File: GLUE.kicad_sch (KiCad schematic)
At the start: 13 parts

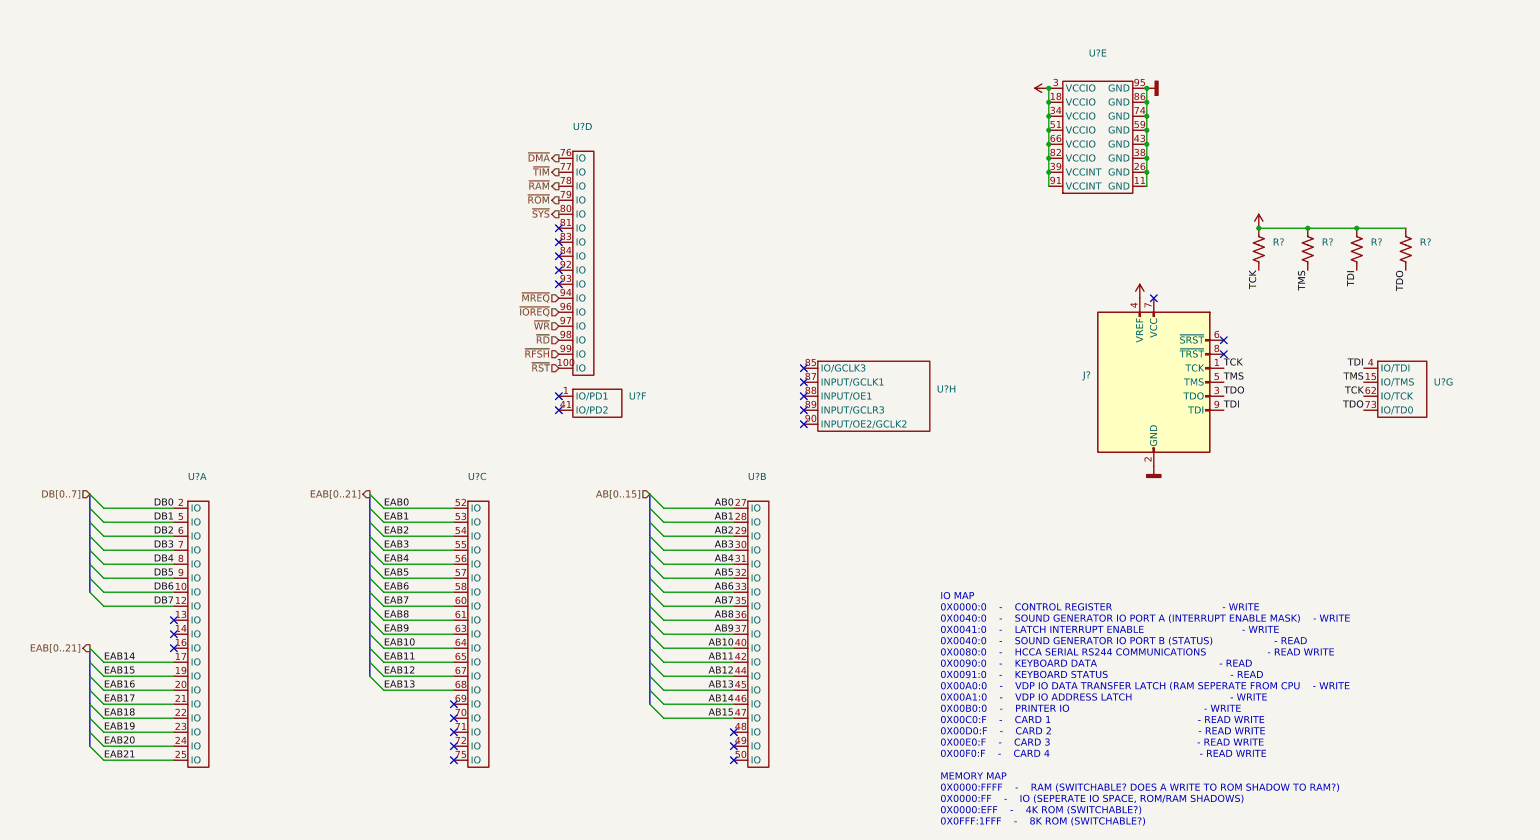
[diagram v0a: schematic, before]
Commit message: updated 84c10 pinout, apparently never checked for validity.... further simplification of dma and timer system (removed mode 2 interrupt structure, and interrupts in general) cleaned up vhdl code for 1508, still need testing to ensure functionality and that it even fits in the 1508....
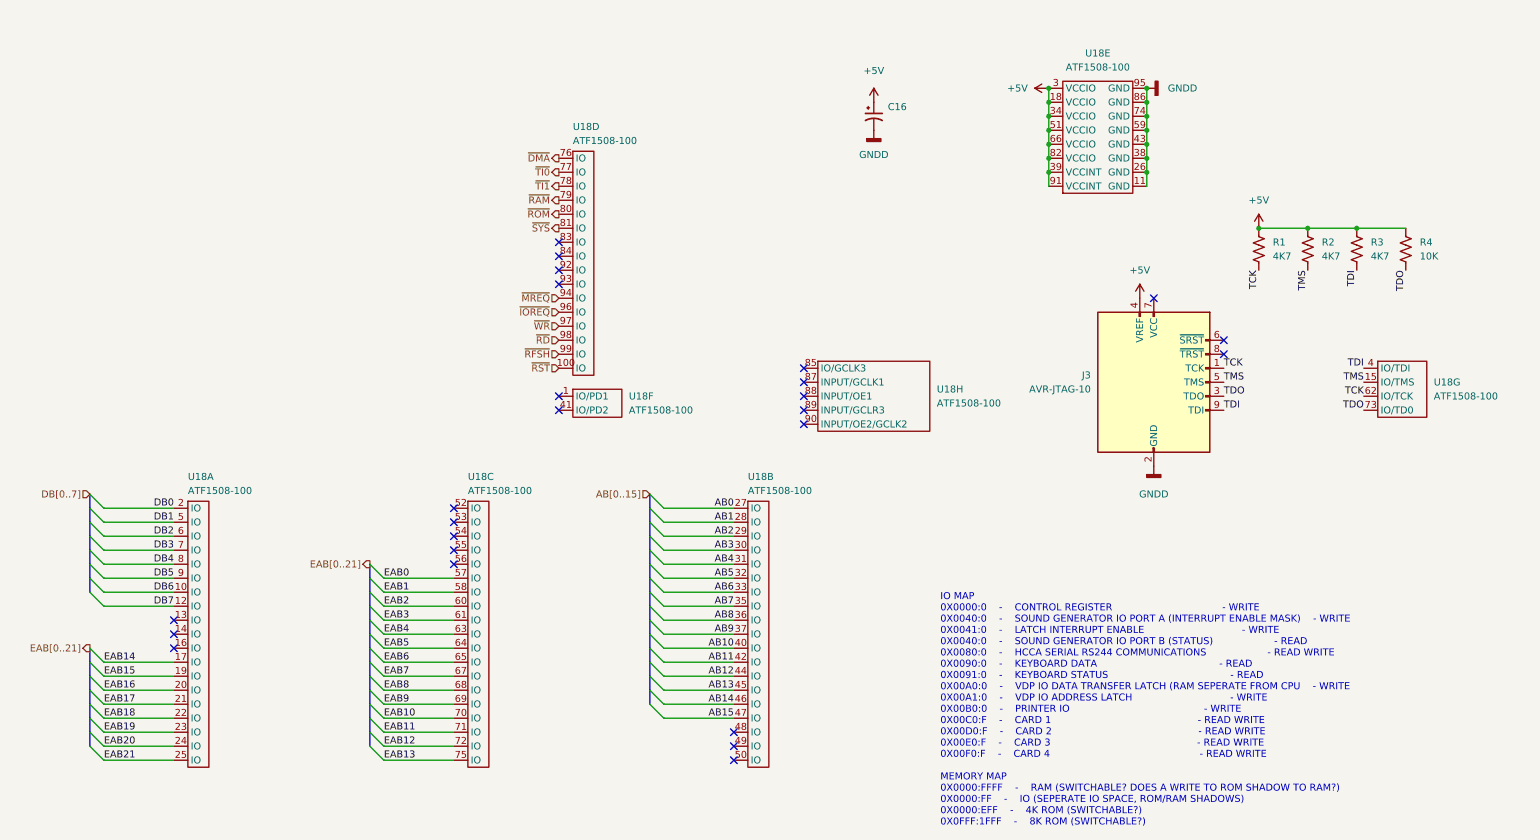
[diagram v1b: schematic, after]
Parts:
- added C16: (no value), symbol Device:C_Polarized_Small_US
- J3: renamed from J?; value (none) -> AVR-JTAG-10; footprint (none) -> Connector_IDC:IDC-Header_2x05_P2.54mm_Horizontal
- R1, R2, R3: renamed from R?; value (none) -> 4K7; footprint (none) -> Resistor_SMD:R_0603_1608Metric
- R4: renamed from R?; value (none) -> 10K; footprint (none) -> Resistor_SMD:R_0603_1608Metric
- U18: renamed from U?; value (none) -> ATF1508-100; footprint (none) -> Package_QFP:TQFP-144_16x16mm_P0.4mm
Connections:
- net +5V: now also C16.1
- net EAB0: now also U18.57 (IO); no longer U18.52 (IO)
- net EAB1: now also U18.58 (IO); no longer U18.53 (IO)
- net EAB10: now also U18.70 (IO); no longer U18.64 (IO)
- net EAB11: now also U18.71 (IO); no longer U18.65 (IO)
- net EAB12: now also U18.72 (IO); no longer U18.67 (IO)
- net EAB13: now also U18.75 (IO); no longer U18.68 (IO)
- net EAB2: now also U18.60 (IO); no longer U18.54 (IO)
- net EAB3: now also U18.61 (IO); no longer U18.55 (IO)
- net EAB4: now also U18.63 (IO); no longer U18.56 (IO)
- net EAB5: now also U18.64 (IO); no longer U18.57 (IO)
- net EAB6: now also U18.65 (IO); no longer U18.58 (IO)
- net EAB7: now also U18.67 (IO); no longer U18.60 (IO)
- net EAB8: now also U18.68 (IO); no longer U18.61 (IO)
- net EAB9: now also U18.69 (IO); no longer U18.63 (IO)
- net GNDD: now also C16.2
- net ~{RAM}: now also U18.79 (IO); no longer U18.78 (IO)
- net ~{ROM}: now also U18.80 (IO); no longer U18.79 (IO)
- net ~{SYS}: now also U18.81 (IO); no longer U18.80 (IO)
- net ~{TIM} renamed ~{TI0}
- new net ~{TI1}: U18.78 (IO)
- no-connect marks 26 -> 25

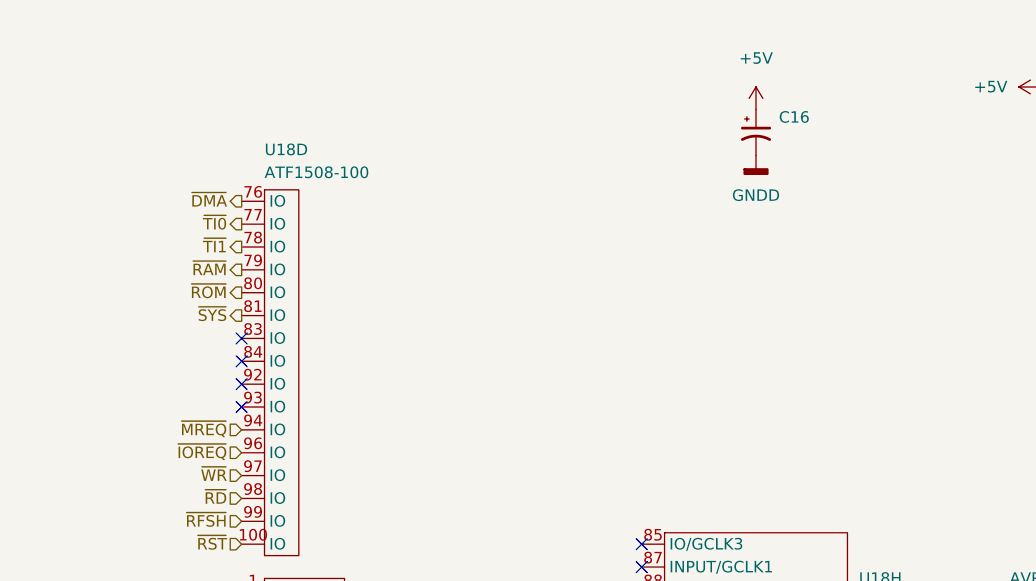
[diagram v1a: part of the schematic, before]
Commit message: forgot to actually add the previous fixes to kicad
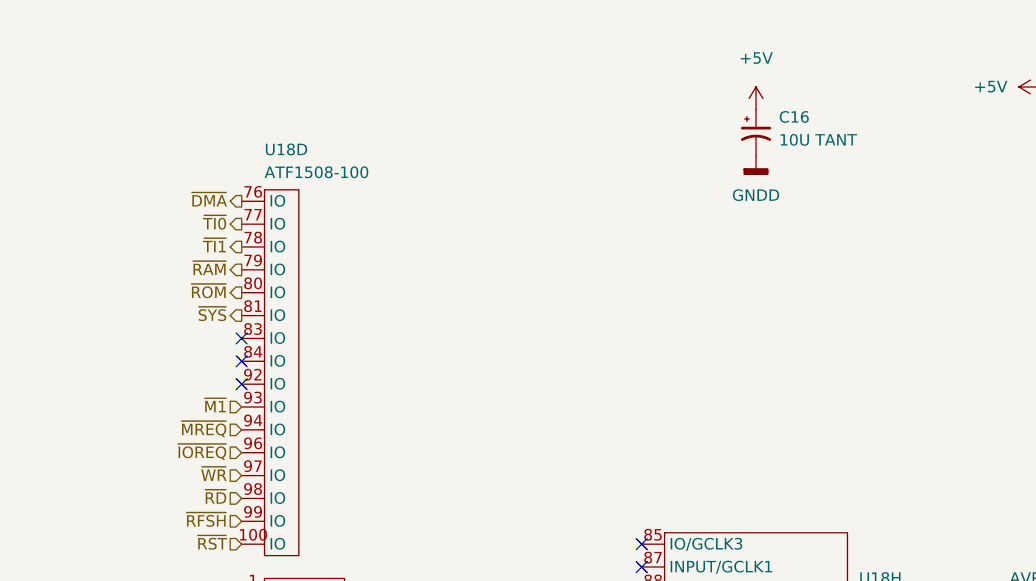
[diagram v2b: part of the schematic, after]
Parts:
- C16: value (none) -> 10U TANT; footprint (none) -> Capacitor_Tantalum_SMD:CP_EIA-3528-15_AVX-H
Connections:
- net ~{M1}: now reaches U18.93 (IO)
- no-connect marks 25 -> 24
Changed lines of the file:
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@@
   (no_connect (at 38.1 128.27))
   (no_connect (at 139.7 153.67))
-  (no_connect (at 107.95 67.31))
   (no_connect (at 88.9 113.03))
   (no_connect (at 107.95 87.63))
@@
     (effects (font (size 1.27 1.27)) (justify right))
   )
+  (hierarchical_label "~{M1}" (shape input) (at 107.95 67.31 180)
+    (effects (font (size 1.27 1.27)) (justify right))
+  )
   (hierarchical_label "~{TI0}" (shape output) (at 107.95 46.99 180)
     (effects (font (size 1.27 1.27)) (justify right))
@@
       (effects (font (size 1.27 1.27)) (justify left))
     )
-    (property "Value" "" (id 1) (at 167.64 37.6681 0)
-      (effects (font (size 1.27 1.27)) (justify left))
-    )
-    (property "Footprint" "" (id 2) (at 165.1 36.83 0)
+    (property "Value" "10U TANT" (id 1) (at 167.64 37.6681 0)
+      (effects (font (size 1.27 1.27)) (justify left))
+    )
+    (property "Footprint" "Capacitor_Tantalum_SMD:CP_EIA-3528-15_AVX-H" (id 2) (at 165.1 36.83 0)
       (effects (font (size 1.27 1.27)) hide)
     )
@@
     (pin "90")
   )
+  (sheet_instances
+    (path "/" (page "1"))
+  )
+  (symbol_instances
+    (path "/7434df1e-8c76-43d0-ba69-cff4ade1af5e"
+      (reference "#PWR094") (unit 1) (value "+5V") (footprint "")
+    )
+    (path "/7de21762-bfdd-4bb2-b954-a7695409df25"
+      (reference "#PWR095") (unit 1) (value "GNDD") (footprint "")
+    )
+    (path "/9c164401-27a9-4d88-be66-43af1a76f3eb"
+      (reference "#PWR096") (unit 1) (value "+5V") (footprint "")
+    )
+    (path "/93ac4910-c1f5-4a01-87b0-acf747d47f0e"
+      (reference "#PWR097") (unit 1) (value "+5V") (footprint "")
+    )
+    (path "/df39298e-6841-46be-bdf6-2826667bc816"
+      (reference "#PWR098") (unit 1) (value "GNDD") (footprint "")
+    )
+    (path "/75ef9d2a-dff4-43fc-9bd8-d0daa9f5c7c0"
+      (reference "#PWR099") (unit 1) (value "GNDD") (footprint "")
+    )
+    (path "/3f1d090d-9c55-4c35-80c5-c0ffce26f264"
+      (reference "#PWR0100") (unit 1) (value "+5V") (footprint "")
+    )
+    (path "/2a6e4ede-8be7-4625-a308-e5070c6ce3b0"
+      (reference "C16") (unit 1) (value "~") (footprint "")
+    )
+    (path "/7dae750f-5ca2-42a0-a992-9bacb9e63901"
+      (reference "J3") (unit 1) (value "AVR-JTAG-10") (footprint "Connector_IDC:IDC-Header_2x05_P2.54mm_Horizontal")
+    )
+    (path "/737b265f-12ab-4831-9a3d-17a7941c355c"
+      (reference "R1") (unit 1) (value "4K7") (footprint "Resistor_SMD:R_0603_1608Metric")
+    )
+    (path "/d143b373-f908-4728-b1a9-27bef0529792"
+      (reference "R2") (unit 1) (value "4K7") (footprint "Resistor_SMD:R_0603_1608Metric")
+    )
+    (path "/5535c419-0d51-45cd-9540-fecebe275496"
+      (reference "R3") (unit 1) (value "4K7") (footprint "Resistor_SMD:R_0603_1608Metric")
+    )
+    (path "/d91b456a-f3e0-43ba-9cb7-46edc063d27a"
+      (reference "R4") (unit 1) (value "10K") (footprint "Resistor_SMD:R_0603_1608Metric")
+    )
+    (path "/eac06b71-dbc2-4ad8-929e-1eb79d804427"
+      (reference "U18") (unit 1) (value "ATF1508-100") (footprint "Package_QFP:TQFP-144_16x16mm_P0.4mm")
+    )
+    (path "/600f8de0-3f16-43a2-b197-38b4e9654d87"
+      (reference "U18") (unit 2) (value "ATF1508-100") (footprint "Package_QFP:TQFP-144_16x16mm_P0.4mm")
+    )
+    (path "/d931fdbc-0cfb-4122-9f70-a852ebf6cf8e"
+      (reference "U18") (unit 3) (value "ATF1508-100") (footprint "Package_QFP:TQFP-144_16x16mm_P0.4mm")
+    )
+    (path "/ec3cefd2-bab6-4b6d-88f5-ba74a67c8eb2"
+      (reference "U18") (unit 4) (value "ATF1508-100") (footprint "Package_QFP:TQFP-144_16x16mm_P0.4mm")
+    )
+    (path "/5b869971-68f3-406b-a43a-58d32abb29a3"
+      (reference "U18") (unit 5) (value "ATF1508-100") (footprint "Package_QFP:TQFP-144_16x16mm_P0.4mm")
+    )
+    (path "/ae7cd84e-81ac-48d4-89cd-9fc94aeaef33"
+      (reference "U18") (unit 6) (value "ATF1508-100") (footprint "Package_QFP:TQFP-144_16x16mm_P0.4mm")
+    )
+    (path "/7199891f-146f-4ca3-92f9-5dadccfd3e4a"
+      (reference "U18") (unit 7) (value "ATF1508-100") (footprint "Package_QFP:TQFP-144_16x16mm_P0.4mm")
+    )
+    (path "/6f075dd7-00c6-4e08-8f3e-01f3ae358f37"
+      (reference "U18") (unit 8) (value "ATF1508-100") (footprint "Package_QFP:TQFP-144_16x16mm_P0.4mm")
+    )
+  )
 )

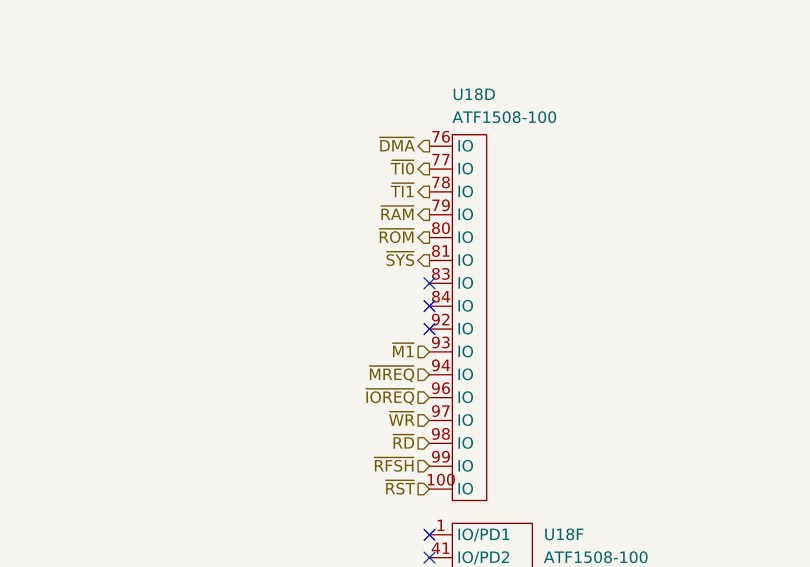
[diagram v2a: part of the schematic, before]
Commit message: fixed logic errors (me being dumb forgetting associativity of ops, and fixed write only system databus on interposer
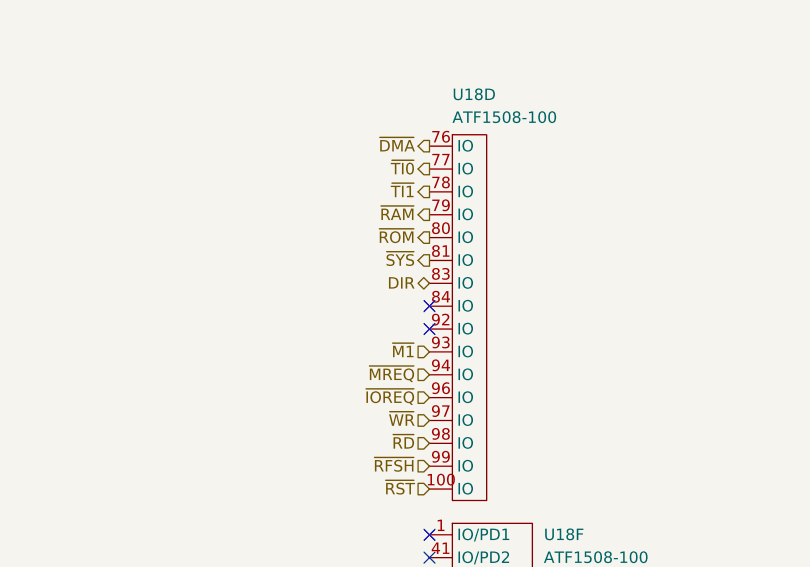
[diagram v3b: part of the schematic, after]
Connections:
- net DIR: now reaches U18.83 (IO)
- no-connect marks 24 -> 23
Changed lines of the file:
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@@
   (no_connect (at 215.9 69.85))
   (no_connect (at 152.4 90.17))
-  (no_connect (at 107.95 59.69))
   (no_connect (at 139.7 148.59))
   (no_connect (at 107.95 62.23))
@@
     (effects (font (size 1.27 1.27)) (justify right))
   )
+  (hierarchical_label "DIR" (shape tri_state) (at 107.95 59.69 180)
+    (effects (font (size 1.27 1.27)) (justify right))
+  )
